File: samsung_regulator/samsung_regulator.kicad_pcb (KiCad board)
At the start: 2 copper layers, 27.9 x 33 mm, 9 parts, among them K1 CONN_3

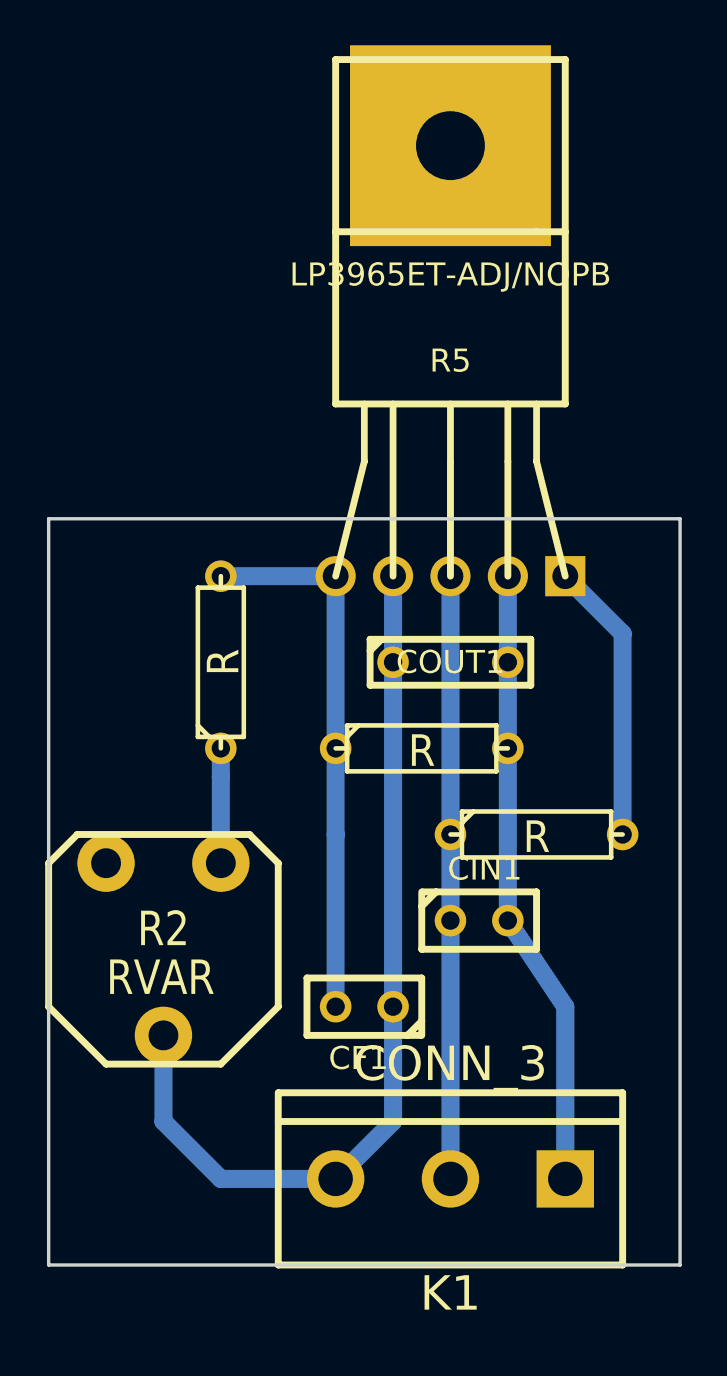
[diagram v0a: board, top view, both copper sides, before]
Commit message: more compact
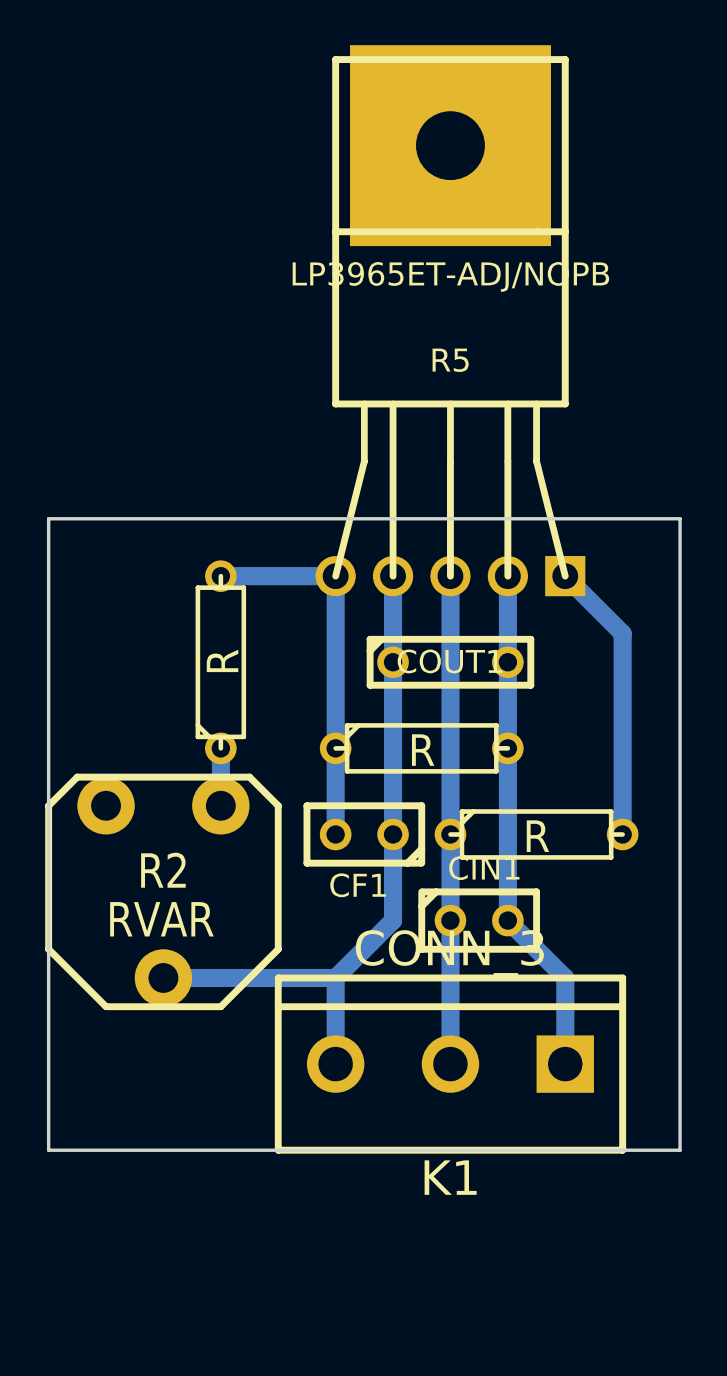
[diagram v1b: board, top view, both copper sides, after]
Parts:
- moved CF1 7.62 mm to (181.6, 82.5)
- moved K1 5.08 mm to (185.4, 92.7)
- moved R2 2.54 mm to (172.7, 85.1)
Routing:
- net N-000004: track 40.2 -> 30.3 mm
- net N-000005: track 24.1 -> 16.5 mm
- net N-000006: track 26.7 -> 21.6 mm
- net GND: track 27.4 -> 22.6 mm
- net N-000002: track 5.08 -> 2.54 mm
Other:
- board size 27.9 x 33 mm -> 27.9 x 27.9 mm
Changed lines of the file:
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@@
     (thickness 1.6)
     (drawings 4)
-    (tracks 23)
+    (tracks 22)
     (zones 0)
     (modules 9)
@@
   )
   (module C1 (layer F.Cu)
-    (at 181.61 90.17 180)
+    (at 181.61 82.55 180)
     (descr "Condensateur e = 1 pas")
     (tags C)
@@
   )
   (module bornier3 (layer F.Cu)
-    (at 185.42 97.79 180)
+    (at 185.42 92.71 180)
     (descr "Bornier d'alimentation 3 pins")
     (tags DEV)
@@
   )
   (module RVAR (layer F.Cu)
-    (at 172.72 87.63 180)
+    (at 172.72 85.09 180)
     (descr "Resistance variable")
     (tags RV)
@@
     )
   )
-  (gr_line (start 195.58 68.58) (end 195.58 101.6) (angle 90) (layer Edge.Cuts) (width 0.15))
+  (gr_line (start 167.64 96.52) (end 167.64 68.58) (angle 90) (layer Edge.Cuts) (width 0.15))
+  (gr_line (start 195.58 68.58) (end 195.58 96.52) (angle 90) (layer Edge.Cuts) (width 0.15))
+  (gr_line (start 195.58 96.52) (end 167.64 96.52) (angle 90) (layer Edge.Cuts) (width 0.15))
   (gr_line (start 167.64 68.58) (end 195.58 68.58) (angle 90) (layer Edge.Cuts) (width 0.15))
-  (gr_line (start 167.64 101.6) (end 167.64 68.58) (angle 90) (layer Edge.Cuts) (width 0.15))
-  (gr_line (start 195.58 101.6) (end 167.64 101.6) (angle 90) (layer Edge.Cuts) (width 0.15))
+  (segment (start 190.5 92.71) (end 190.5 88.9) (width 0.8) (layer B.Cu) (net 1) (status 400000))
+  (segment (start 190.5 88.9) (end 187.96 86.36) (width 0.8) (layer B.Cu) (net 1) (status 800000))
   (segment (start 187.96 71.12) (end 187.96 74.93) (width 0.8) (layer B.Cu) (net 1))
   (segment (start 187.96 74.93) (end 187.96 78.74) (width 0.8) (layer B.Cu) (net 1) (status 10))
   (segment (start 187.96 78.74) (end 187.96 86.36) (width 0.8) (layer B.Cu) (net 1) (status 10))
-  (segment (start 190.5 97.79) (end 190.5 90.17) (width 0.8) (layer B.Cu) (net 1))
-  (segment (start 190.5 90.17) (end 187.96 86.36) (width 0.8) (layer B.Cu) (net 1) (status 20))
-  (segment (start 175.26 83.82) (end 175.26 80.01) (width 0.8) (layer B.Cu) (net 2))
+  (segment (start 175.26 81.28) (end 175.26 80.01) (width 0.8) (layer B.Cu) (net 2) (status 10))
   (segment (start 175.26 80.01) (end 175.26 78.74) (width 0.8) (layer B.Cu) (net 2) (status 20))
   (segment (start 190.5 71.12) (end 193.04 73.66) (width 0.8) (layer B.Cu) (net 3))
   (segment (start 193.04 73.66) (end 193.04 82.55) (width 0.8) (layer B.Cu) (net 3))
-  (segment (start 172.72 91.44) (end 172.72 95.25) (width 0.8) (layer B.Cu) (net 4))
-  (segment (start 175.26 97.79) (end 180.34 97.79) (width 0.8) (layer B.Cu) (net 4))
-  (segment (start 172.72 95.25) (end 175.26 97.79) (width 0.8) (layer B.Cu) (net 4))
+  (segment (start 180.34 88.9) (end 182.88 86.36) (width 0.8) (layer B.Cu) (net 4))
+  (segment (start 182.88 86.36) (end 182.88 82.55) (width 0.8) (layer B.Cu) (net 4) (status 800000))
+  (segment (start 182.88 82.55) (end 182.88 74.93) (width 0.8) (layer B.Cu) (net 4) (status C00000))
+  (segment (start 172.72 88.9) (end 180.34 88.9) (width 0.8) (layer B.Cu) (net 4) (status 400000))
+  (segment (start 180.34 92.71) (end 180.34 88.9) (width 0.8) (layer B.Cu) (net 4) (status 400000))
   (segment (start 182.88 74.93) (end 182.88 71.12) (width 0.8) (layer B.Cu) (net 4))
-  (segment (start 182.88 74.93) (end 182.88 90.17) (width 0.8) (layer B.Cu) (net 4) (status 10))
-  (segment (start 182.88 90.17) (end 182.88 95.25) (width 0.8) (layer B.Cu) (net 4) (status 10))
-  (segment (start 182.88 95.25) (end 180.34 97.79) (width 0.8) (layer B.Cu) (net 4))
-  (segment (start 175.26 71.12) (end 180.34 71.12) (width 0.8) (layer B.Cu) (net 5) (status C00000))
+  (segment (start 175.26 71.12) (end 180.34 71.12) (width 0.8) (layer B.Cu) (net 5))
   (segment (start 180.34 78.74) (end 180.34 71.12) (width 0.8) (layer B.Cu) (net 5))
-  (segment (start 180.34 90.17) (end 180.34 82.55) (width 0.8) (layer B.Cu) (net 5) (status 20))
+  (segment (start 180.34 82.55) (end 180.34 82.55) (width 0.8) (layer B.Cu) (net 5) (status 10))
   (segment (start 180.34 82.55) (end 180.34 78.74) (width 0.8) (layer B.Cu) (net 5) (status 10))
+  (segment (start 185.42 92.71) (end 185.42 86.36) (width 0.8) (layer B.Cu) (net 6) (status C00000))
   (segment (start 185.42 82.55) (end 185.42 71.12) (width 0.8) (layer B.Cu) (net 6))
-  (segment (start 185.42 97.79) (end 185.42 86.36) (width 0.8) (layer B.Cu) (net 6) (status 20))
   (segment (start 185.42 86.36) (end 185.42 82.55) (width 0.8) (layer B.Cu) (net 6) (status 10))
 )
